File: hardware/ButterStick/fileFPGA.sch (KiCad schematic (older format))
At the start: 3 parts, among them U3 ECP5U25, X1 ASDMB

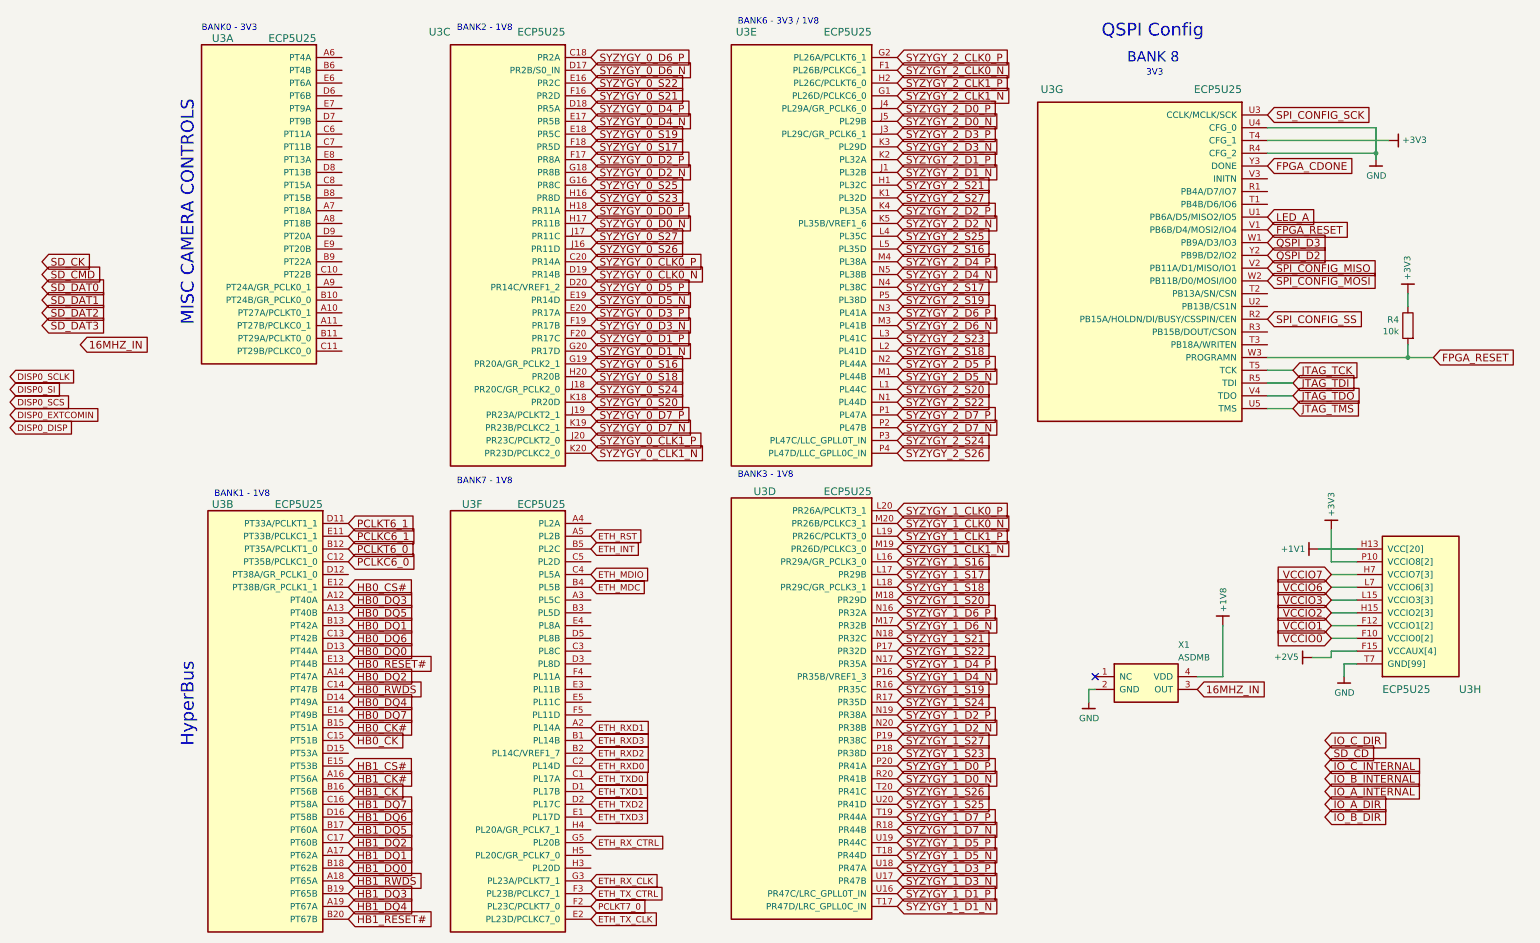
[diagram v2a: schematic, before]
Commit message: Update schematic hieracy layout.
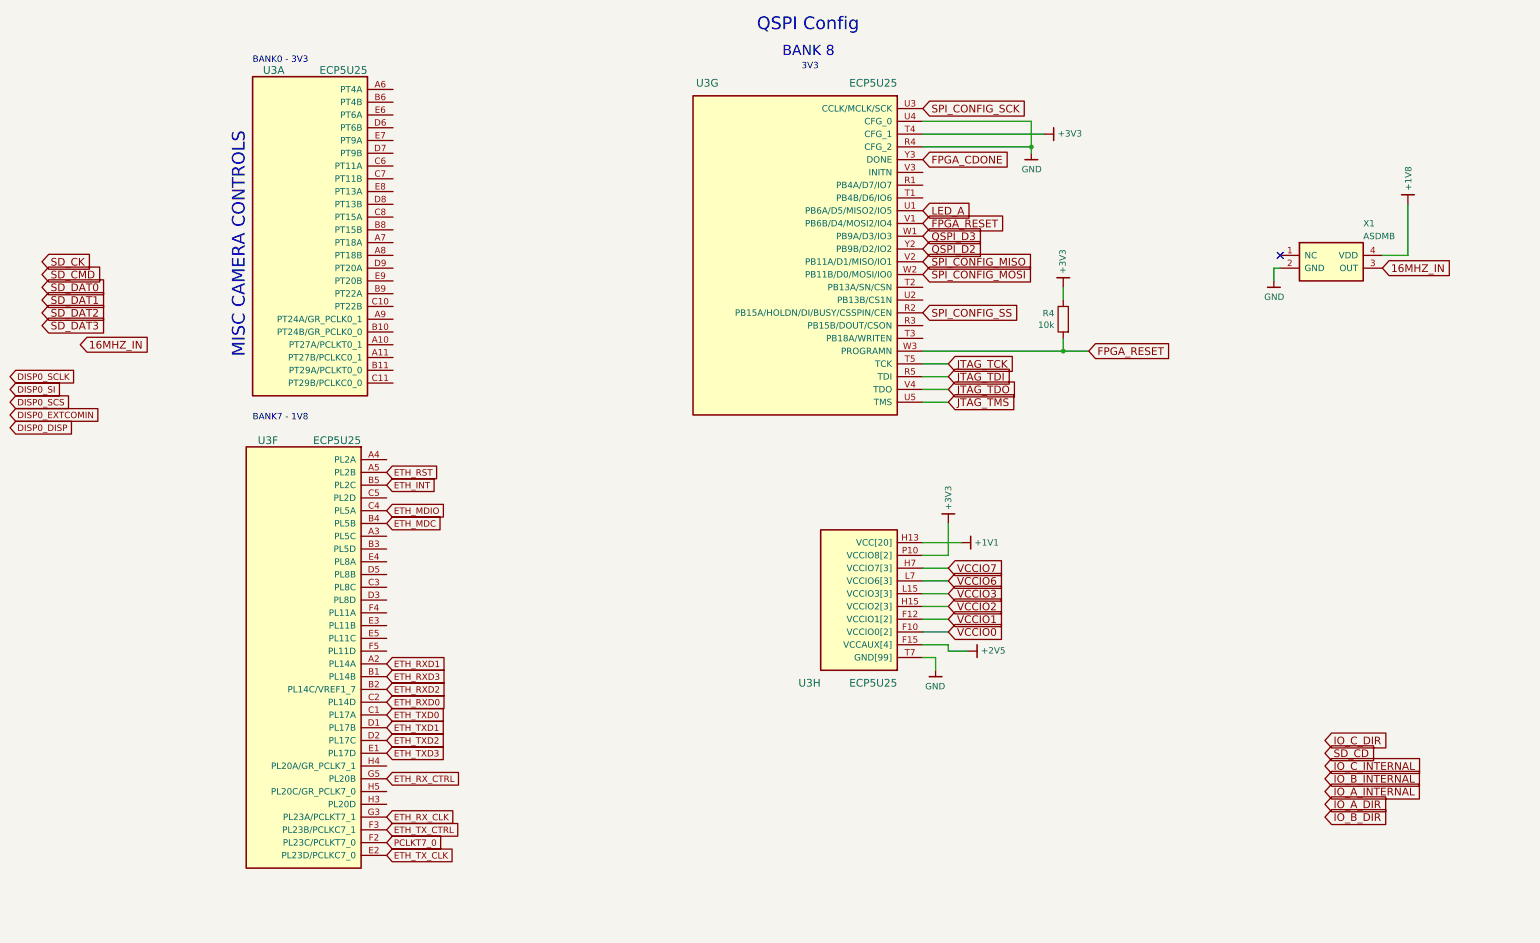
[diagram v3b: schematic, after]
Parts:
- removed unit 2 of U3
- removed unit 5 of U3
- removed unit 3 of U3
- removed unit 4 of U3
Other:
- note removed: "BANK1 - 1V8"
- note removed: "BANK2 - 1V8"
- note removed: "BANK3 - 1V8"
- note removed: "BANK6 - 3V3 / 1V8\n"
- note removed: "HyperBus"
- moved on the sheet: R4, U3A, U3F, U3G, U3H, X1

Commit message: Routed all SYZYGY ports. Placed decoupling caps etc.
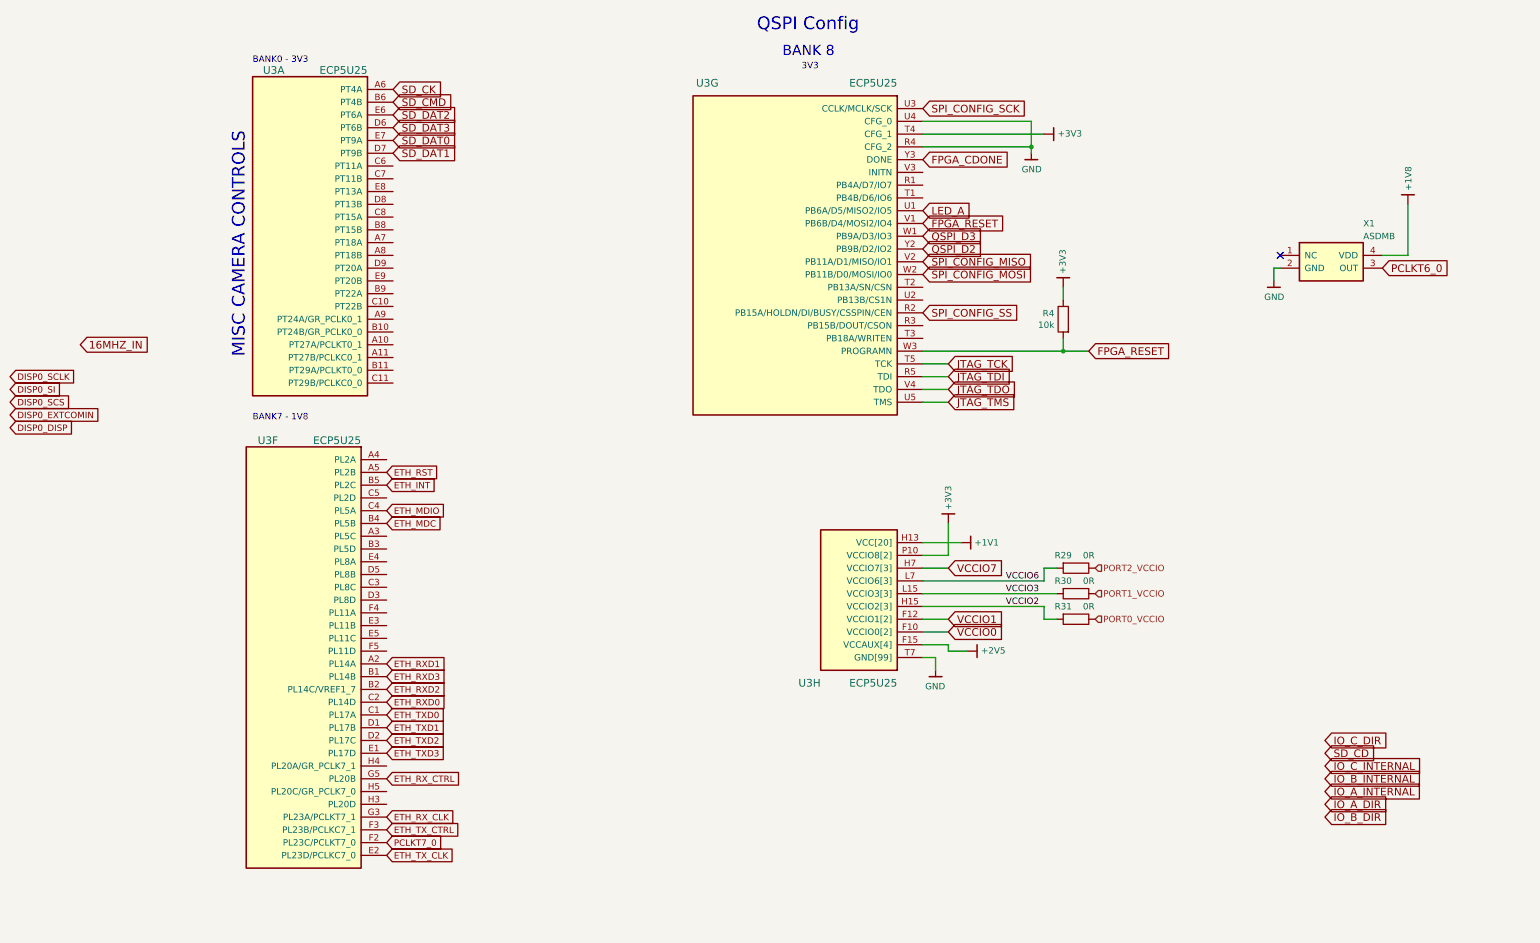
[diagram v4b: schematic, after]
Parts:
- added R29, R30, R31: 0R, pkl_dipol:R_0402, symbol Device:R
- U3: footprint (none) -> gkl_housings_bga:caBGA_381_17x17
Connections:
- net 16MHZ_IN: no longer X1.3 (OUT)
- net SD_CK: now also U3.A6 (PT4A)
- net SD_CMD: now also U3.B6 (PT4B)
- net SD_DAT0: now also U3.E7 (PT9A)
- net SD_DAT1: now also U3.D7 (PT9B)
- net SD_DAT2: now also U3.E6 (PT6A)
- net SD_DAT3: now also U3.D6 (PT6B)
- net VCCIO2: now also R31.2
- net VCCIO3: now also R30.2
- net VCCIO6: now also R29.2
- new net PCLKT6_0: X1.3 (OUT)
- new net PORT0_VCCIO: R31.1
- new net PORT1_VCCIO: R30.1
- new net PORT2_VCCIO: R29.1
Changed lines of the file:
@@
 $Descr A4 11693 8268
 encoding utf-8
-Sheet 2 13
+Sheet 2 14
 Title ""
 Date ""
@@
 Text GLabel 6450 1650 2    60   Input ~ 0
 FPGA_CDONE
-Text GLabel -450 2650 2    60   Input ~ 0
+Text GLabel 2300 1500 2    60   Input ~ 0
 SD_DAT0
-Text GLabel -450 2750 2    60   Input ~ 0
+Text GLabel 2300 1600 2    60   Input ~ 0
 SD_DAT1
-Text GLabel -450 2850 2    60   Input ~ 0
+Text GLabel 2300 1300 2    60   Input ~ 0
 SD_DAT2
-Text GLabel -450 2950 2    60   Input ~ 0
+Text GLabel 2300 1400 2    60   Input ~ 0
 SD_DAT3
-Text GLabel -450 2550 2    60   Input ~ 0
+Text GLabel 2300 1200 2    60   Input ~ 0
 SD_CMD
-Text GLabel -450 2450 2    60   Input ~ 0
+Text GLabel 2300 1100 2    60   Input ~ 0
 SD_CK
 Text GLabel 9600 6300 2    60   Input ~ 0
@@
 Wire Wire Line
 	10250 2400 10250 2000
-Text GLabel 10050 2500 2    60   Input ~ 0
-16MHZ_IN
 $Comp
 L Device:R R4
@@
 F 0 "U3" H 3150 1250 60  0000 L CNN
 F 1 "ECP5U25" H 2500 1250 60  0000 L CNN
-F 2 "" H 2300 1100 50  0001 C CNN
+F 2 "gkl_housings_bga:caBGA_381_17x17" H 2300 1100 50  0001 C CNN
 F 3 "" H 2300 1100 50  0001 C CNN
 F 4 " 220-2052-ND " H 400 250 50  0001 C CNN "SN-DK"
@@
 F 0 "U3" H 3100 4150 60  0000 L CNN
 F 1 "ECP5U25" H 2450 4150 60  0000 L CNN
-F 2 "" H 2250 4000 50  0001 C CNN
+F 2 "gkl_housings_bga:caBGA_381_17x17" H 2250 4000 50  0001 C CNN
 F 3 "" H 2250 4000 50  0001 C CNN
 F 4 " 220-2052-ND " H 350 -350 50  0001 C CNN "SN-DK"
@@
 F 0 "U3" H 8050 1450 60  0000 L CNN
 F 1 "ECP5U25" H 6650 1450 60  0000 L CNN
-F 2 "" H 6450 1250 50  0001 C CNN
+F 2 "gkl_housings_bga:caBGA_381_17x17" H 6450 1250 50  0001 C CNN
 F 3 "" H 6450 1250 50  0001 C CNN
 F 4 " 220-2052-ND " H -2700 -50 50  0001 C CNN "SN-DK"
@@
 F 0 "U3" H 7250 5750 60  0000 L CNN
 F 1 "ECP5U25" H 6650 5750 60  0000 L CNN
-F 2 "" H 6450 5550 50  0001 C CNN
+F 2 "gkl_housings_bga:caBGA_381_17x17" H 6450 5550 50  0001 C CNN
 F 3 "" H 6450 5550 50  0001 C CNN
 F 4 " 220-2052-ND " H -3400 -50 50  0001 C CNN "SN-DK"
@@
 Text GLabel 6650 5250 2    60   Input ~ 0
 VCCIO1
-Text GLabel 6650 5150 2    60   Input ~ 0
-VCCIO2
-Text GLabel 6650 5050 2    60   Input ~ 0
-VCCIO3
 Text GLabel 6650 4850 2    60   Input ~ 0
 VCCIO7
-Text GLabel 6650 4950 2    60   Input ~ 0
-VCCIO6
 Wire Wire Line
 	6800 5500 6650 5500
@@
 Wire Wire Line
 	6650 4850 6450 4850
-Wire Wire Line
-	6650 4950 6450 4950
-Wire Wire Line
-	6650 5050 6450 5050
-Wire Wire Line
-	6650 5150 6450 5150
 Wire Wire Line
 	6650 5250 6450 5250
@@
 	9200 2500 9250 2500
 NoConn ~ 9250 2400
+Text HLabel 7800 5250 2    50   Input ~ 0
+PORT0_VCCIO
+Text HLabel 7800 5050 2    50   Input ~ 0
+PORT1_VCCIO
+Text HLabel 7800 4850 2    50   Input ~ 0
+PORT2_VCCIO
+$Comp
+L Device:R R29
+U 1 1 5C9CDF63
+P 7650 4850
+F 0 "R29" V 7550 4750 50  0000 C CNN
+F 1 "0R" V 7550 4950 50  0000 C CNN
+F 2 "pkl_dipol:R_0402" V 7580 4850 50  0001 C CNN
+F 3 "~" H 7650 4850 50  0001 C CNN
+	1    7650 4850
+	0    1    1    0
+$EndComp
+$Comp
+L Device:R R30
+U 1 1 5C9CE4FB
+P 7650 5050
+F 0 "R30" V 7550 4950 50  0000 C CNN
+F 1 "0R" V 7550 5150 50  0000 C CNN
+F 2 "pkl_dipol:R_0402" V 7580 5050 50  0001 C CNN
+F 3 "~" H 7650 5050 50  0001 C CNN
+	1    7650 5050
+	0    1    1    0
+$EndComp
+$Comp
+L Device:R R31
+U 1 1 5C9CEE6F
+P 7650 5250
+F 0 "R31" V 7550 5150 50  0000 C CNN
+F 1 "0R" V 7550 5350 50  0000 C CNN
+F 2 "pkl_dipol:R_0402" V 7580 5250 50  0001 C CNN
+F 3 "~" H 7650 5250 50  0001 C CNN
+	1    7650 5250
+	0    1    1    0
+$EndComp
+Wire Wire Line
+	7400 4950 7400 4850
+Wire Wire Line
+	7400 4850 7500 4850
+Wire Wire Line
+	6450 4950 7400 4950
+Wire Wire Line
+	6450 5050 7500 5050
+Wire Wire Line
+	7400 5150 7400 5250
+Wire Wire Line
+	7400 5250 7500 5250
+Wire Wire Line
+	6450 5150 7400 5150
+Text Label 7100 4950 0    50   ~ 0
+VCCIO6
+Text Label 7100 5050 0    50   ~ 0
+VCCIO3
+Text Label 7100 5150 0    50   ~ 0
+VCCIO2
+Text GLabel 10050 2500 2    60   Input ~ 0
+PCLKT6_0
 $EndSCHEMATC

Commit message: Added ESD on SD card signals.
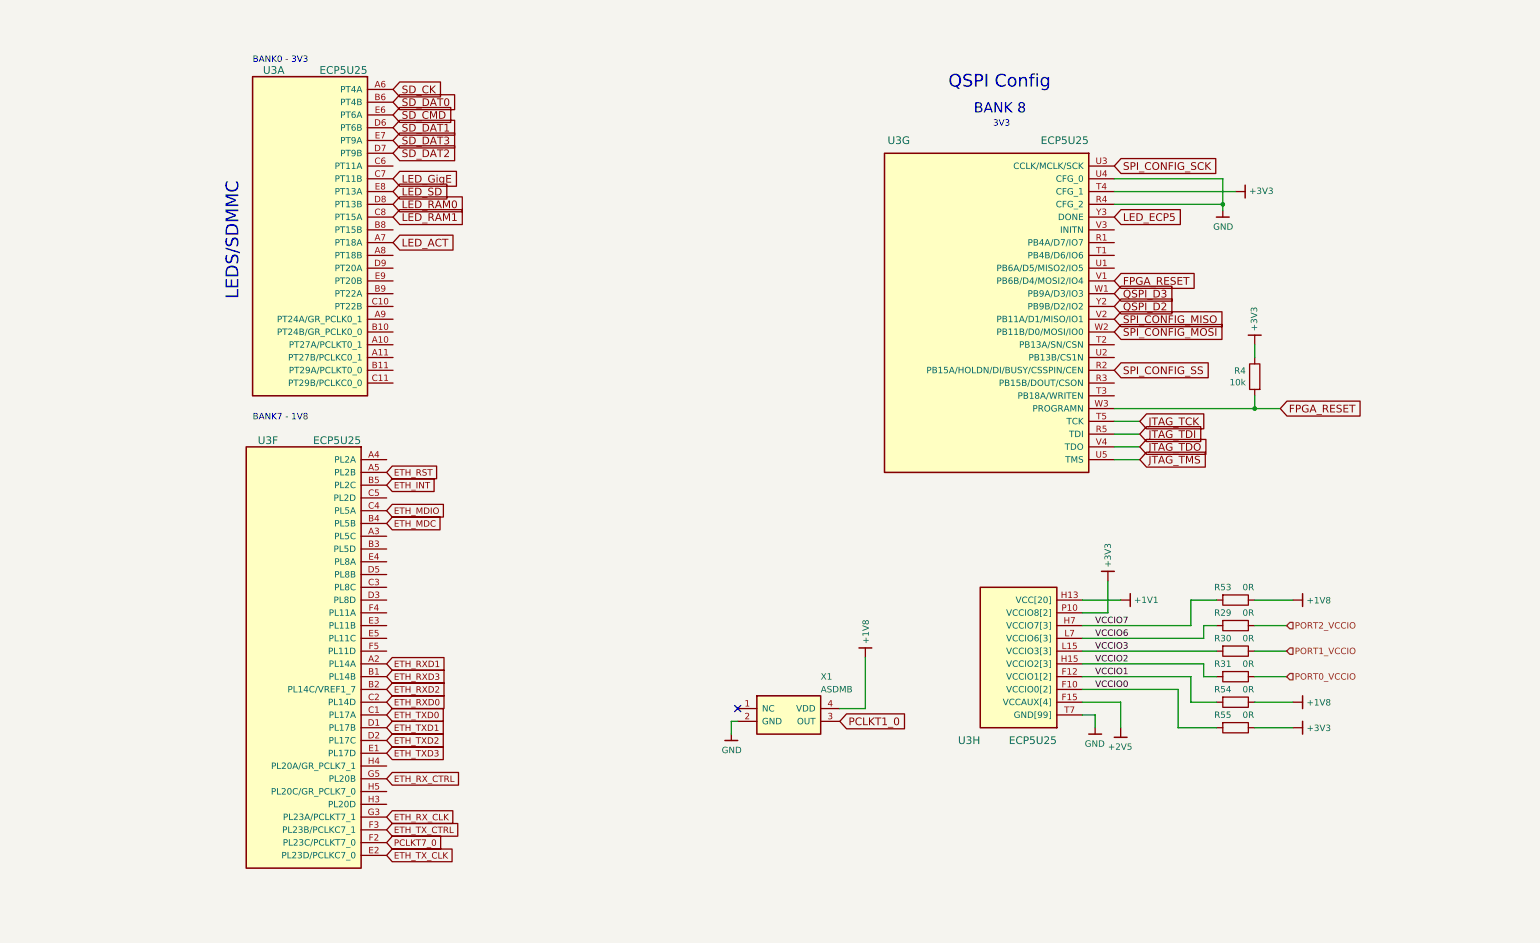
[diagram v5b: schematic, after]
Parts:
- added R53, R54, R55: 0R, pkl_dipol:R_0402, symbol Device:R
- R4: footprint Resistors_SMD:R_0402 -> pkl_dipol:R_0402
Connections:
- net +1V8: now also R53.1, R54.1
- net +3V3: now also R55.1
- net SD_CMD: now also U3.E6 (PT6A); no longer U3.B6 (PT4B)
- net SD_DAT0: now also U3.B6 (PT4B); no longer U3.E7 (PT9A)
- net SD_DAT1: now also U3.D6 (PT6B); no longer U3.D7 (PT9B)
- net SD_DAT2: now also U3.D7 (PT9B); no longer U3.E6 (PT6A)
- net SD_DAT3: now also U3.E7 (PT9A); no longer U3.D6 (PT6B)
- net VCCIO0: now also R55.2
- net VCCIO1: now also R54.2
- net VCCIO7: now also R53.2
- net LED_ACT: now reaches U3.A7 (PT18A)
- net LED_GigE: now reaches U3.C7 (PT11B)
- net LED_RAM1: now reaches U3.C8 (PT15A)
- net LED_RAM0: now reaches U3.D8 (PT13B)
- net LED_SD: now reaches U3.E8 (PT13A)
- net FPGA_CDONE renamed LED_ECP5
- net LED_A: no longer names the net of U3.U1 (PB6A/D5/MISO2/IO5)
- net PCLKT6_0 renamed PCLKT1_0
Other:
- note added: "LEDS/SDMMC\n"
- note removed: "MISC CAMERA CONTROLS\n"
- moved on the sheet: R29, R30, R31, R4, U3G, U3H, X1

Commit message: Update KiCad PCB.
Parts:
- U3: PN LFE5U-25F-6BG381I -> LFE5U-45F-8BG381C
- X1: MFG (none) -> SiTIME; PN SIT8008BI-71-18E-24.000000G -> SIT8008BI-73-18S-25.000000G
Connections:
- net SD_CD: now reaches U3.C6 (PT11A)
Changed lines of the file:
@@
 F 3 "http://www.abracon.com/Oscillators/ASV.pdf" H 5300 6000 50  0001 C CNN
 F 4 " 1473-30509-1-ND " H -3000 150 50  0001 C CNN "SN-DK"
-F 5 " SIT8008BI-71-18E-24.000000G " H -3000 150 50  0001 C CNN "PN"
+F 5 "SIT8008BI-73-18S-25.000000G" H -3000 150 50  0001 C CNN "PN"
+F 6 "SiTIME" H 0   0   50  0001 C CNN "MFG"
 	1    5400 6000
 	1    0    0    -1
@@
 F 3 "" H 2300 1100 50  0001 C CNN
 F 4 " 220-2052-ND " H 400 250 50  0001 C CNN "SN-DK"
-F 5 " LFE5U-25F-6BG381I " H 400 250 50  0001 C CNN "PN"
+F 5 "LFE5U-45F-8BG381C" H 400 250 50  0001 C CNN "PN"
 F 6 "Lattice" H 400 250 50  0001 C CNN "Mfg"
 	1    2300 1100
@@
 F 3 "" H 2250 4000 50  0001 C CNN
 F 4 " 220-2052-ND " H 350 -350 50  0001 C CNN "SN-DK"
-F 5 " LFE5U-25F-6BG381I " H 350 -350 50  0001 C CNN "PN"
+F 5 "LFE5U-45F-8BG381C" H 350 -350 50  0001 C CNN "PN"
 F 6 "Lattice" H 350 -350 50  0001 C CNN "Mfg"
 	6    2250 4000
@@
 F 3 "" H 7950 1700 50  0001 C CNN
 F 4 " 220-2052-ND " H -1200 400 50  0001 C CNN "SN-DK"
-F 5 " LFE5U-25F-6BG381I " H -1200 400 50  0001 C CNN "PN"
+F 5 "LFE5U-45F-8BG381C" H -1200 400 50  0001 C CNN "PN"
 F 6 "Lattice" H -1200 400 50  0001 C CNN "Mfg"
 	7    7950 1700
@@
 F 3 "" H 7700 6000 50  0001 C CNN
 F 4 " 220-2052-ND " H -2150 400 50  0001 C CNN "SN-DK"
-F 5 " LFE5U-25F-6BG381I " H -2150 400 50  0001 C CNN "PN"
+F 5 "LFE5U-45F-8BG381C" H -2150 400 50  0001 C CNN "PN"
 F 6 "Lattice" H -2150 400 50  0001 C CNN "Mfg"
 	8    7700 6000
@@
 Wire Wire Line
 	7700 5300 8550 5300
+Text GLabel 2300 1700 2    60   Input ~ 0
+SD_CD
 $EndSCHEMATC

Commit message: Finalised part values update BOM values to reflect. Swapped layers 4/5 due to stackup changes
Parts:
- R29, R30, R31, R53, R54, R55: Mfg (none) -> Stackpole Electronics Inc; PN (none) -> RMCF0402ZT0R00
- R4: Mfg (none) -> Stackpole Electronics Inc; PN ERA-2AED103X -> RMCF0402FT10K0
- X1: PN SIT8008BI-73-18S-25.000000G -> SIT8008BI-72-18N-25.000000G
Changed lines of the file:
@@
 EESchema Schematic File Version 4
 LIBS:ButterStick-cache
-EELAYER 26 0
+EELAYER 29 0
 EELAYER END
 $Descr A4 11693 8268
 encoding utf-8
 Sheet 2 13
-Title ""
-Date ""
-Rev ""
-Comp ""
+Title "ButterStick"
+Date "2019-03-19"
+Rev "r0_1"
+Comp "GsD"
 Comment1 ""
 Comment2 ""
@@
 F 3 "http://www.abracon.com/Oscillators/ASV.pdf" H 5300 6000 50  0001 C CNN
 F 4 " 1473-30509-1-ND " H -3000 150 50  0001 C CNN "SN-DK"
-F 5 "SIT8008BI-73-18S-25.000000G" H -3000 150 50  0001 C CNN "PN"
+F 5 "SIT8008BI-72-18N-25.000000G" H -3000 150 50  0001 C CNN "PN"
 F 6 "SiTIME" H 0   0   50  0001 C CNN "MFG"
 	1    5400 6000
@@
 F 3 "" H 9050 3350 50  0001 C CNN
 F 4 "P10KDECT-ND" H -1200 800 50  0001 C CNN "SN-DK"
-F 5 "ERA-2AED103X" H -1200 800 50  0001 C CNN "PN"
+F 5 "RMCF0402FT10K0" H -1200 800 50  0001 C CNN "PN"
+F 6 "Stackpole Electronics Inc" H 0   0   50  0001 C CNN "Mfg"
 	1    9050 3350
 	-1   0    0    -1
@@
 F 2 "pkl_dipol:R_0402" V 8830 5300 50  0001 C CNN
 F 3 "~" H 8900 5300 50  0001 C CNN
+F 4 "Stackpole Electronics Inc" H 0   0   50  0001 C CNN "Mfg"
+F 5 "RMCF0402ZT0R00" H 0   0   50  0001 C CNN "PN"
 	1    8900 5300
 	0    1    1    0
@@
 F 2 "pkl_dipol:R_0402" V 8830 5500 50  0001 C CNN
 F 3 "~" H 8900 5500 50  0001 C CNN
+F 4 "Stackpole Electronics Inc" H 0   0   50  0001 C CNN "Mfg"
+F 5 "RMCF0402ZT0R00" H 0   0   50  0001 C CNN "PN"
 	1    8900 5500
 	0    1    1    0
@@
 F 2 "pkl_dipol:R_0402" V 8830 5700 50  0001 C CNN
 F 3 "~" H 8900 5700 50  0001 C CNN
+F 4 "Stackpole Electronics Inc" H 0   0   50  0001 C CNN "Mfg"
+F 5 "RMCF0402ZT0R00" H 0   0   50  0001 C CNN "PN"
 	1    8900 5700
 	0    1    1    0
@@
 F 2 "pkl_dipol:R_0402" V 8830 5900 50  0001 C CNN
 F 3 "~" H 8900 5900 50  0001 C CNN
+F 4 "Stackpole Electronics Inc" H 0   0   50  0001 C CNN "Mfg"
+F 5 "RMCF0402ZT0R00" H 0   0   50  0001 C CNN "PN"
 	1    8900 5900
 	0    1    1    0
@@
 F 2 "pkl_dipol:R_0402" V 8830 6100 50  0001 C CNN
 F 3 "~" H 8900 6100 50  0001 C CNN
+F 4 "Stackpole Electronics Inc" H 0   0   50  0001 C CNN "Mfg"
+F 5 "RMCF0402ZT0R00" H 0   0   50  0001 C CNN "PN"
 	1    8900 6100
 	0    1    1    0
@@
 F 2 "pkl_dipol:R_0402" V 8830 5100 50  0001 C CNN
 F 3 "~" H 8900 5100 50  0001 C CNN
+F 4 "Stackpole Electronics Inc" H 0   0   50  0001 C CNN "Mfg"
+F 5 "RMCF0402ZT0R00" H 0   0   50  0001 C CNN "PN"
 	1    8900 5100
 	0    1    1    0
